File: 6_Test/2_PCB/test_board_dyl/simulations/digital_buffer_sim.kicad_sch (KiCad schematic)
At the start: 4 parts, among them U1 SN74ALVCH162827DLR

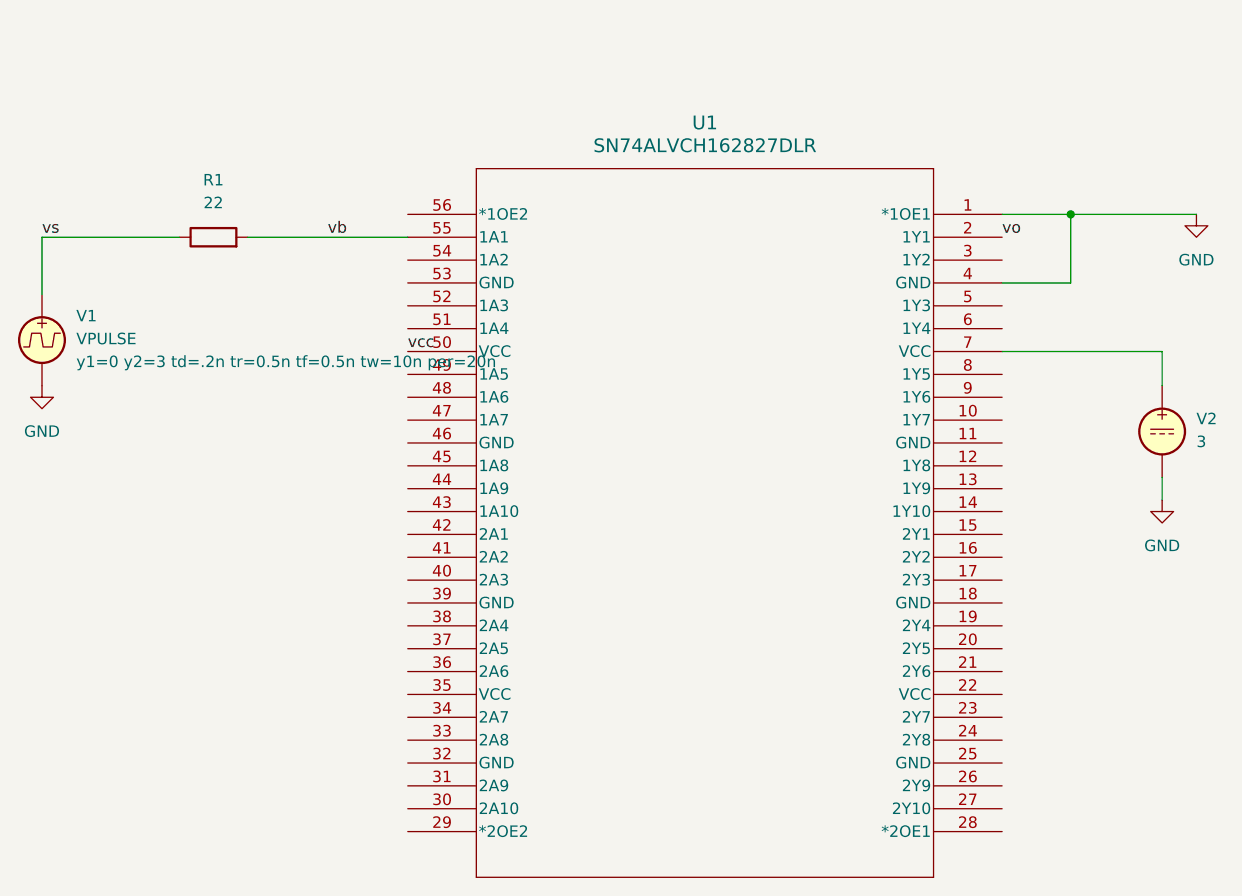
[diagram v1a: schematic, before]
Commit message: Digital Buffer Simulation
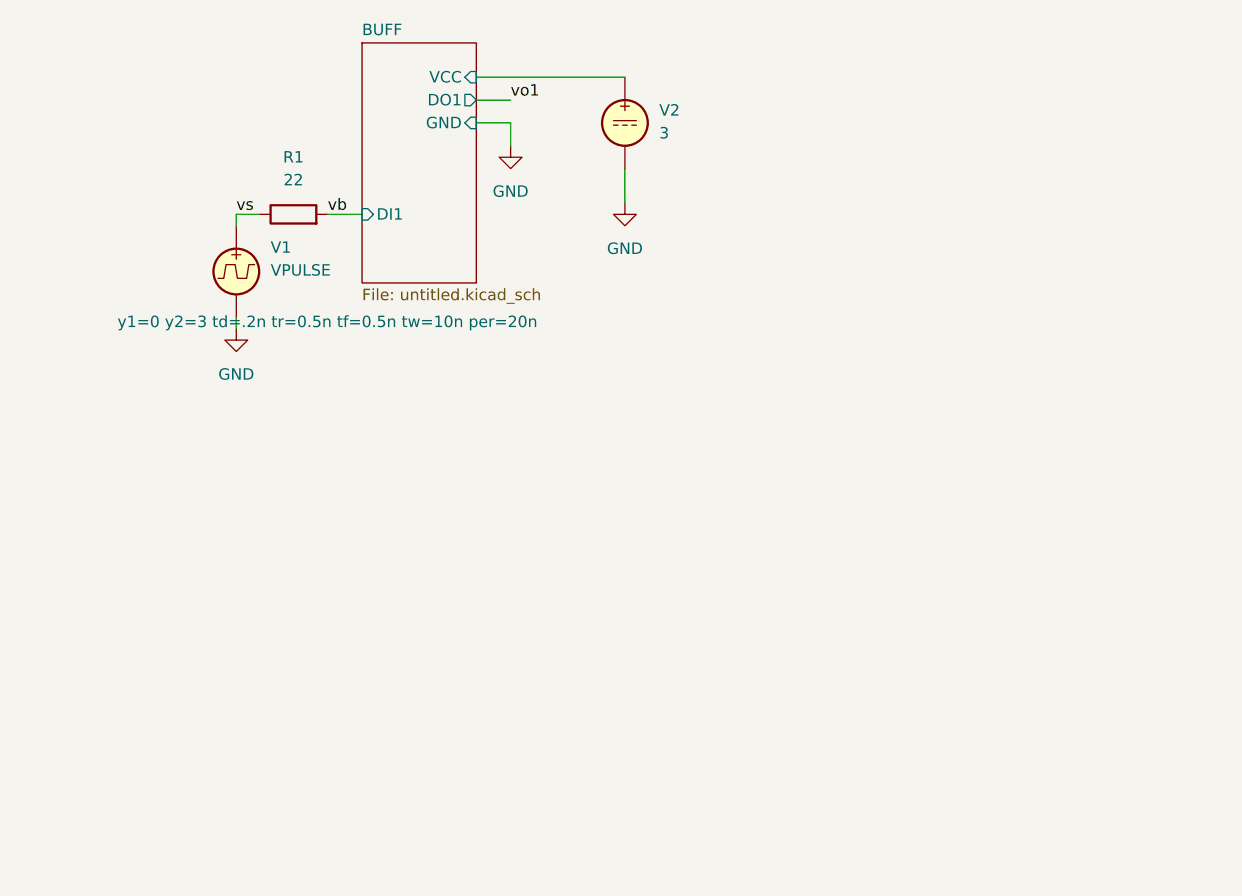
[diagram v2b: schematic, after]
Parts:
- removed U1: SN74ALVCH162827DLR, DL56, symbol buffer:SN74ALVCH162827DLR
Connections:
- net BUFF/VCC: now reaches V2.1
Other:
- added sheet BUFF (untitled.kicad_sch)
- moved on the sheet: R1, V1, V2
